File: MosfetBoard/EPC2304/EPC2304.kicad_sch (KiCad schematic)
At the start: 4 parts, among them J2 LogicConnector

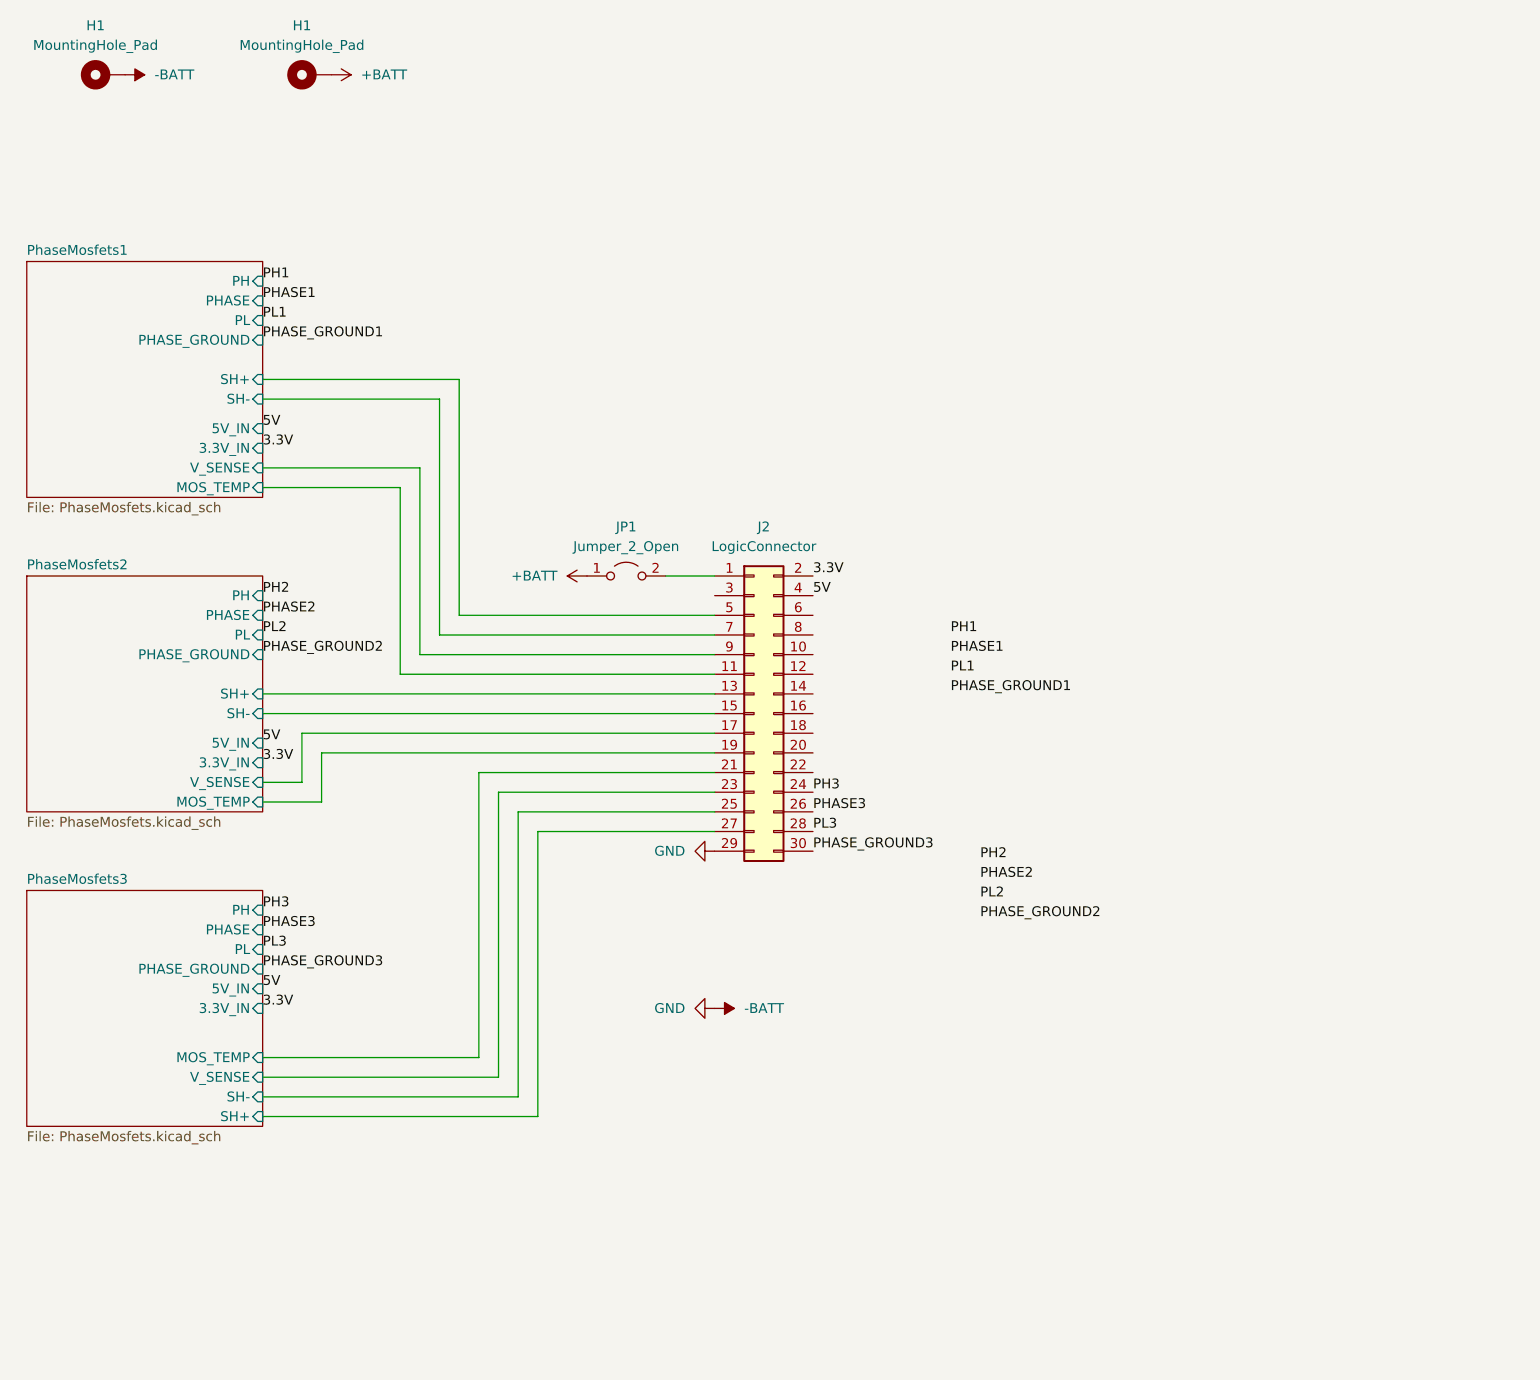
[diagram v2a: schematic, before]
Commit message: v3.0.1 - GaN redesign
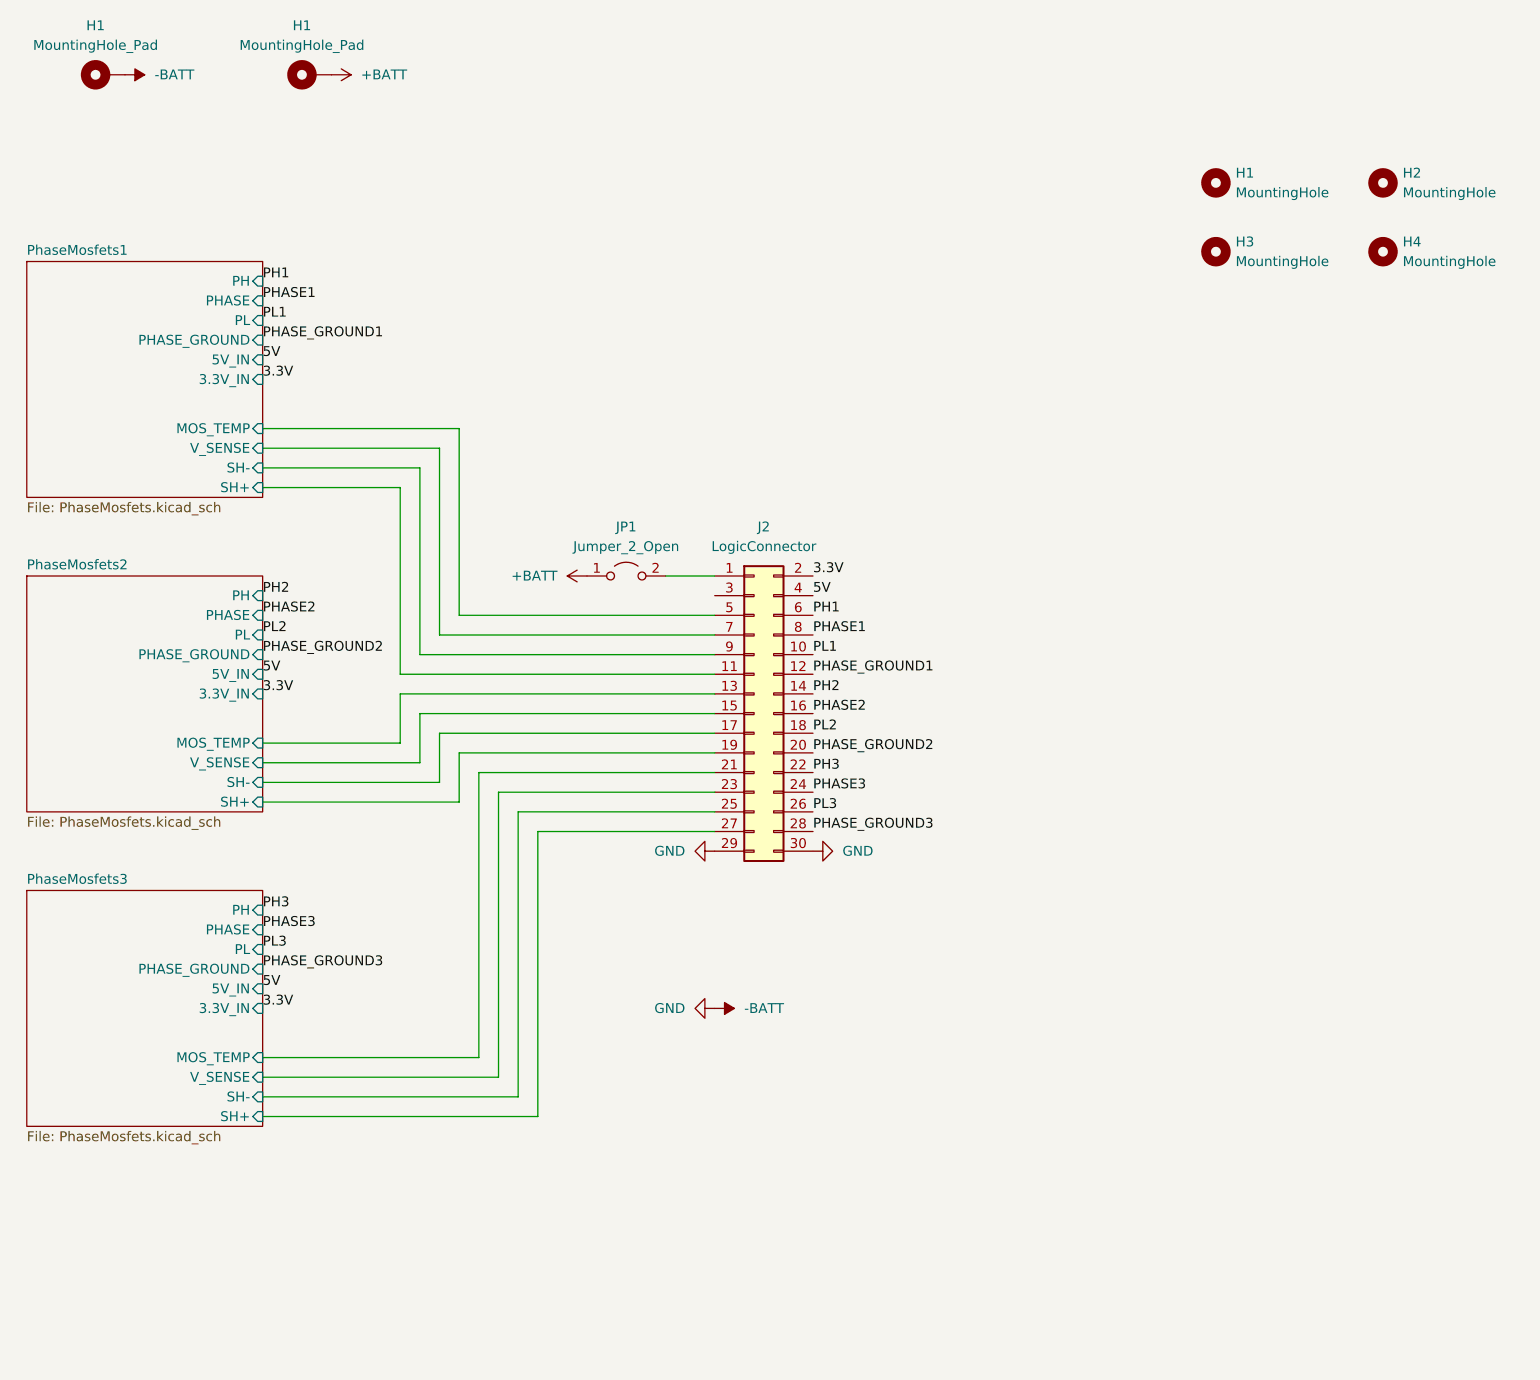
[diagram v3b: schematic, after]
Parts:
- added H1, H2, H3, H4: MountingHole, MountingHole:MountingHole_3.2mm_M3_ISO14580, symbol Mechanical:MountingHole
- JP1: footprint (none) -> GigaVescLibs:SolderJumper0.5mm_Open
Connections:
- net -BATT: now also J2.30 (Pin_30)
- net PH1: now also J2.6 (Pin_6)
- net PH2: now also J2.14 (Pin_14)
- net PH3: now also J2.22 (Pin_22); no longer J2.24 (Pin_24)
- net PHASE1: now also J2.8 (Pin_8)
- net PHASE2: now also J2.16 (Pin_16)
- net PHASE3: now also J2.24 (Pin_24); no longer J2.26 (Pin_26)
- net PHASE_GROUND1: now also J2.12 (Pin_12)
- net PHASE_GROUND2: now also J2.20 (Pin_20)
- net PHASE_GROUND3: now also J2.28 (Pin_28); no longer J2.30 (Pin_30)
- net PL1: now also J2.10 (Pin_10)
- net PL2: now also J2.18 (Pin_18)
- net PL3: now also J2.26 (Pin_26); no longer J2.28 (Pin_28)
- net PhaseMosfets1/MOS_TEMP: now also J2.5 (Pin_5); no longer J2.11 (Pin_11)
- net PhaseMosfets1/SH+: now also J2.11 (Pin_11); no longer J2.5 (Pin_5)
- net PhaseMosfets1/SH-: now also J2.9 (Pin_9); no longer J2.7 (Pin_7)
- net PhaseMosfets1/V_SENSE: now also J2.7 (Pin_7); no longer J2.9 (Pin_9)
- net PhaseMosfets2/MOS_TEMP: now also J2.13 (Pin_13); no longer J2.19 (Pin_19)
- net PhaseMosfets2/SH+: now also J2.19 (Pin_19); no longer J2.13 (Pin_13)
- net PhaseMosfets2/SH-: now also J2.17 (Pin_17); no longer J2.15 (Pin_15)
- net PhaseMosfets2/V_SENSE: now also J2.15 (Pin_15); no longer J2.17 (Pin_17)

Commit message: v3.0.2 - Prerelease
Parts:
- J2: JLCPosOffset (none) -> 17.78,-1.27; JLCRotOffset (none) -> -90; MPN (none) -> C2685203
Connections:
- net PhaseMosfets1/V_SENSE: no longer names the net of J2.7 (Pin_7)
- net PhaseMosfets2/V_SENSE: no longer names the net of J2.15 (Pin_15)
- net PhaseMosfets3/V_SENSE: no longer names the net of J2.23 (Pin_23)
- no-connect marks 0 -> 4
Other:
- sheet PhaseMosfets1 ports: added none; removed V_SENSE
- sheet PhaseMosfets2 ports: added none; removed V_SENSE
- sheet PhaseMosfets3 ports: added none; removed V_SENSE
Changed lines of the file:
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@@
 (kicad_sch (version 20230121) (generator eeschema)
   (paper "A4")
-  (wire (pts (xy 83.82 119.38) (xy 83.82 156.21))
-    (stroke (width 0) (type default))
-  )
+  (no_connect (at 111.76 93.98))
+  (no_connect (at 111.76 99.06))
+  (no_connect (at 111.76 119.38))
+  (no_connect (at 111.76 109.22))
   (wire (pts (xy 71.12 113.03) (xy 71.12 106.68))
     (stroke (width 0) (type default))
@@
     (stroke (width 0) (type default))
   )
-  (wire (pts (xy 76.2 74.93) (xy 76.2 99.06))
-    (stroke (width 0) (type default))
-  )
-  (wire (pts (xy 73.66 109.22) (xy 111.76 109.22))
-    (stroke (width 0) (type default))
-  )
   (wire (pts (xy 53.34 118.11) (xy 76.2 118.11))
     (stroke (width 0) (type default))
@@
     (stroke (width 0) (type default))
   )
-  (wire (pts (xy 53.34 156.21) (xy 83.82 156.21))
-    (stroke (width 0) (type default))
-  )
-  (wire (pts (xy 76.2 99.06) (xy 111.76 99.06))
-    (stroke (width 0) (type default))
-  )
   (wire (pts (xy 53.34 161.29) (xy 88.9 161.29))
     (stroke (width 0) (type default))
@@
     (stroke (width 0) (type default))
   )
-  (wire (pts (xy 53.34 115.57) (xy 73.66 115.57))
-    (stroke (width 0) (type default))
-  )
   (wire (pts (xy 78.74 120.65) (xy 78.74 114.3))
     (stroke (width 0) (type default))
   )
-  (wire (pts (xy 73.66 115.57) (xy 73.66 109.22))
-    (stroke (width 0) (type default))
-  )
   (wire (pts (xy 88.9 124.46) (xy 111.76 124.46))
     (stroke (width 0) (type default))
@@
   )
   (wire (pts (xy 73.66 101.6) (xy 111.76 101.6))
-    (stroke (width 0) (type default))
-  )
-  (wire (pts (xy 53.34 74.93) (xy 76.2 74.93))
-    (stroke (width 0) (type default))
-  )
-  (wire (pts (xy 111.76 119.38) (xy 83.82 119.38))
     (stroke (width 0) (type default))
   )
@@
     )
     (property "Datasheet" "~" (at 116.84 109.22 0)
+      (effects (font (size 1.27 1.27)) hide)
+    )
+    (property "JLCRotOffset" "-90" (at 116.84 109.22 0)
+      (effects (font (size 1.27 1.27)) hide)
+    )
+    (property "MPN" "C2685203" (at 116.84 109.22 0)
+      (effects (font (size 1.27 1.27)) hide)
+    )
+    (property "JLCPosOffset" "17.78,-1.27" (at 116.84 109.22 0)
       (effects (font (size 1.27 1.27)) hide)
     )
@@
       (effects (font (size 1.27 1.27)) (justify right))
     )
-    (pin "V_SENSE" input (at 53.34 74.93 0)
-      (effects (font (size 1.27 1.27)) (justify right))
-    )
     (pin "SH+" input (at 53.34 80.01 0)
       (effects (font (size 1.27 1.27)) (justify right))
@@
       (effects (font (size 1.27 1.27)) (justify right))
     )
-    (pin "V_SENSE" input (at 53.34 156.21 0)
-      (effects (font (size 1.27 1.27)) (justify right))
-    )
     (pin "SH+" input (at 53.34 161.29 0)
       (effects (font (size 1.27 1.27)) (justify right))
@@
       (effects (font (size 1.27 1.27)) (justify right))
     )
-    (pin "V_SENSE" input (at 53.34 115.57 0)
-      (effects (font (size 1.27 1.27)) (justify right))
-    )

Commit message: EPC board update
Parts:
- renumbered H1 to H4, H1 to H6

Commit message: v3.3.3 - EPC pcb revised
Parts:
- H1, H2, H3, H4: footprint MountingHole:MountingHole_3.2mm_M3_ISO14580 -> GigaVescLibs:CapHead_3.5mm
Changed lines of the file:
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@@
 			)
 		)
-		(property "Footprint" "MountingHole:MountingHole_3.2mm_M3_ISO14580"
+		(property "Footprint" "GigaVescLibs:CapHead_3.5mm"
 			(at 176.53 40.64 0)
 			(effects
@@
 			)
 		)
-		(property "Footprint" "MountingHole:MountingHole_3.2mm_M3_ISO14580"
+		(property "Footprint" "GigaVescLibs:CapHead_3.5mm"
 			(at 198.12 40.64 0)
 			(effects
@@
 			)
 		)
-		(property "Footprint" "MountingHole:MountingHole_3.2mm_M3_ISO14580"
+		(property "Footprint" "GigaVescLibs:CapHead_3.5mm"
 			(at 198.12 49.53 0)
 			(effects
@@
 			)
 		)
-		(property "Footprint" "MountingHole:MountingHole_3.2mm_M3_ISO14580"
+		(property "Footprint" "GigaVescLibs:CapHead_3.5mm"
 			(at 176.53 49.53 0)
 			(effects
